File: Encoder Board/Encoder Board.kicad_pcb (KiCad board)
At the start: 2 copper layers, 62.2 x 52.8 mm, 20 parts, among them J1 Conn_02x05_Odd_Even, J2 Conn_02x05_Odd_Even, J3 Conn_01x02_Pin, J4 Conn_01x02_Pin, J5 Conn_01x20, J6 Conn_01x20, J7 Conn_02x04_Odd_Even, U1 AM26LV32xD

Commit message: routing
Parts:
- moved C1 2.41 mm to (68.5, 51.2)
- moved R1 1.97 mm to (65.4, 52.1)
- moved C4 0.72 mm to (75.1, 54.3)
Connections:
- C2 pad 1: /B_N -> /INDEX_N
- C3 pad 1: /INDEX_N -> /B_N
- J5 pad 5: /B_3V3 -> /INDEX_3V3
- J5 pad 6: /INDEX_3V3 -> /B_3V3
- R2 pad 2: /B -> /INDEX
- R3 pad 2: /INDEX -> /B
- U1 pad 10: /INDEX -> /B
- U1 pad 11: /INDEX_3V3 -> /B_3V3
- U1 pad 5: /B_3V3 -> /INDEX_3V3
- U1 pad 6: /B -> /INDEX
- U1 pad 7: /B_N -> /INDEX_N
- U1 pad 9: /INDEX_N -> /B_N
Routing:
- net /B_N: track 48.7 -> 97.4 mm, vias 0 -> 1
- net /B: track 54.3 -> 97.1 mm, vias 0 -> 1
- net /A: track 62.0 -> 83.5 mm
- net /INDEX_3V3: track 5.75 -> 24.5 mm, vias 0 -> 2
- net /INDEX_N: track 61.1 -> 77.9 mm
- net /INDEX: track 68.6 -> 80.5 mm
- net /A_3V3: track 14.9 -> 23.6 mm, vias 1 -> 2
- net /A_N: track 67.3 -> 73.2 mm
- net +3V3: track 1.14 -> 6.99 mm
- net /B_3V3: track 14.1 -> 18.5 mm
- net GND: track 2.54 -> 0.00 mm, vias 38 -> 37

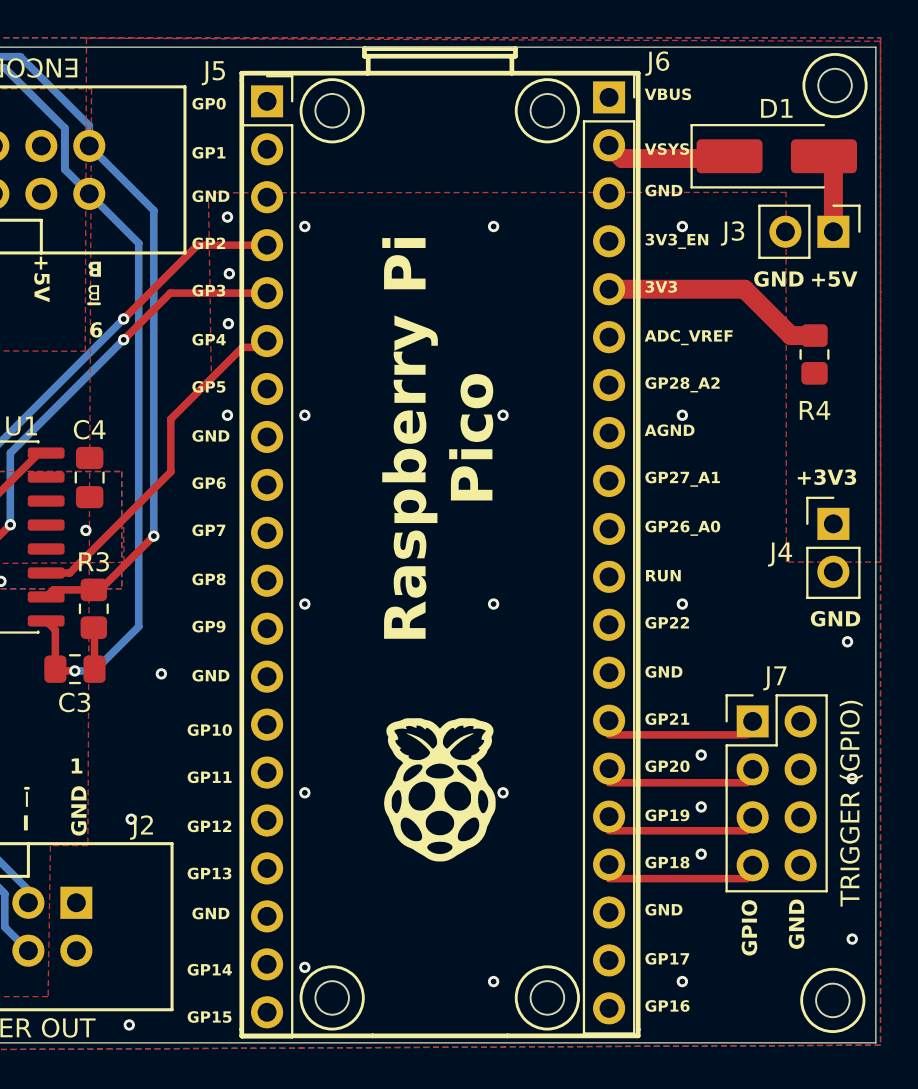
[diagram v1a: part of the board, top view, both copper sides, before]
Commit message: fix silkscreen
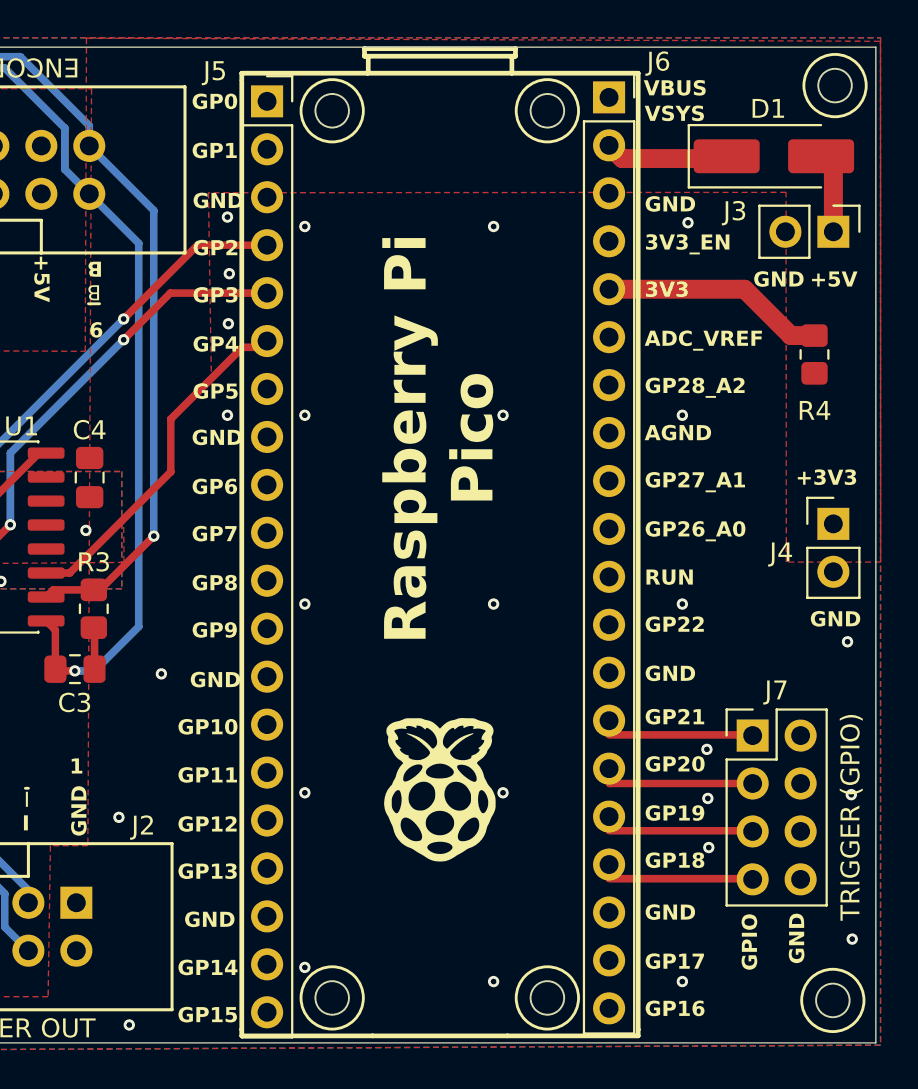
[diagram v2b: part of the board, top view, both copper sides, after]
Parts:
- moved J7 0.75 mm to (110.2, 68.0)
- moved D1 0.15 mm to (111.3, 37.3)
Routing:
- net Net-(J6-Pin_15): track 7.36 -> 7.94 mm

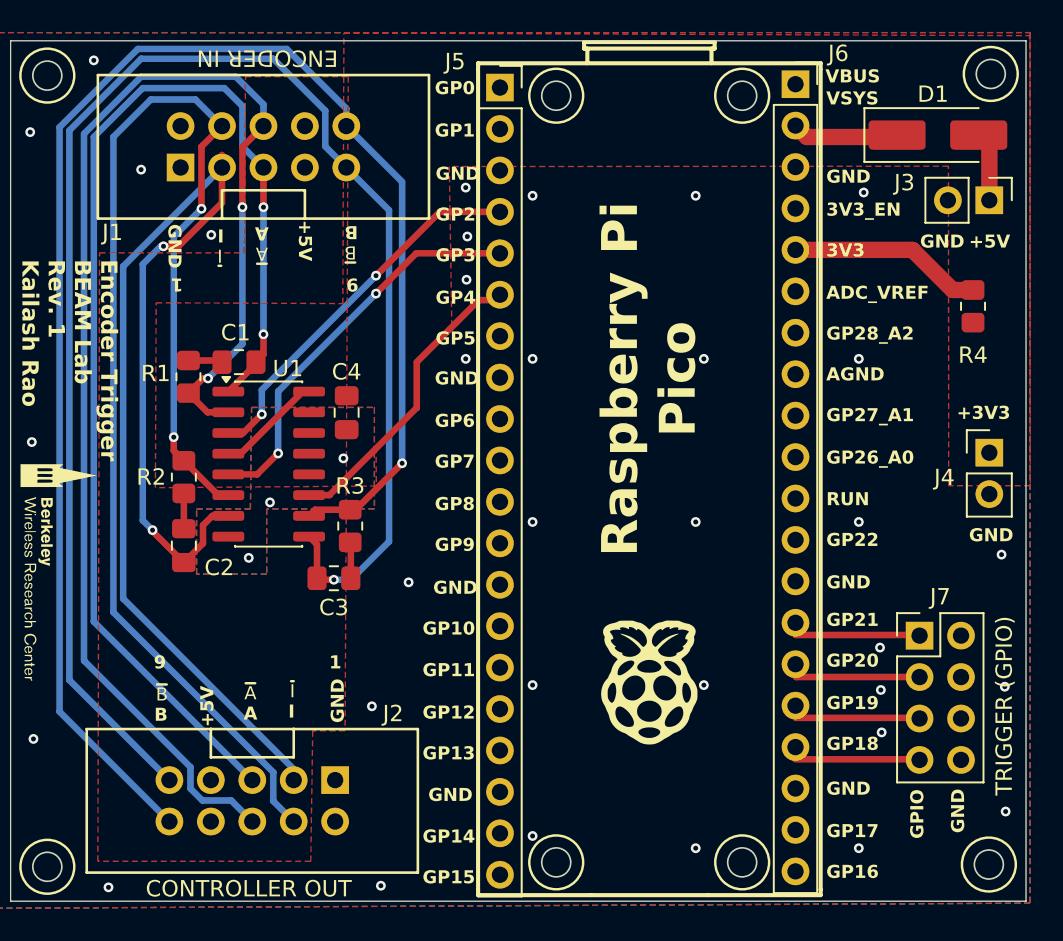
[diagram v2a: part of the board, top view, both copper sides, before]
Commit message: fix J7 connections, C4/U1 decoupling cap connection
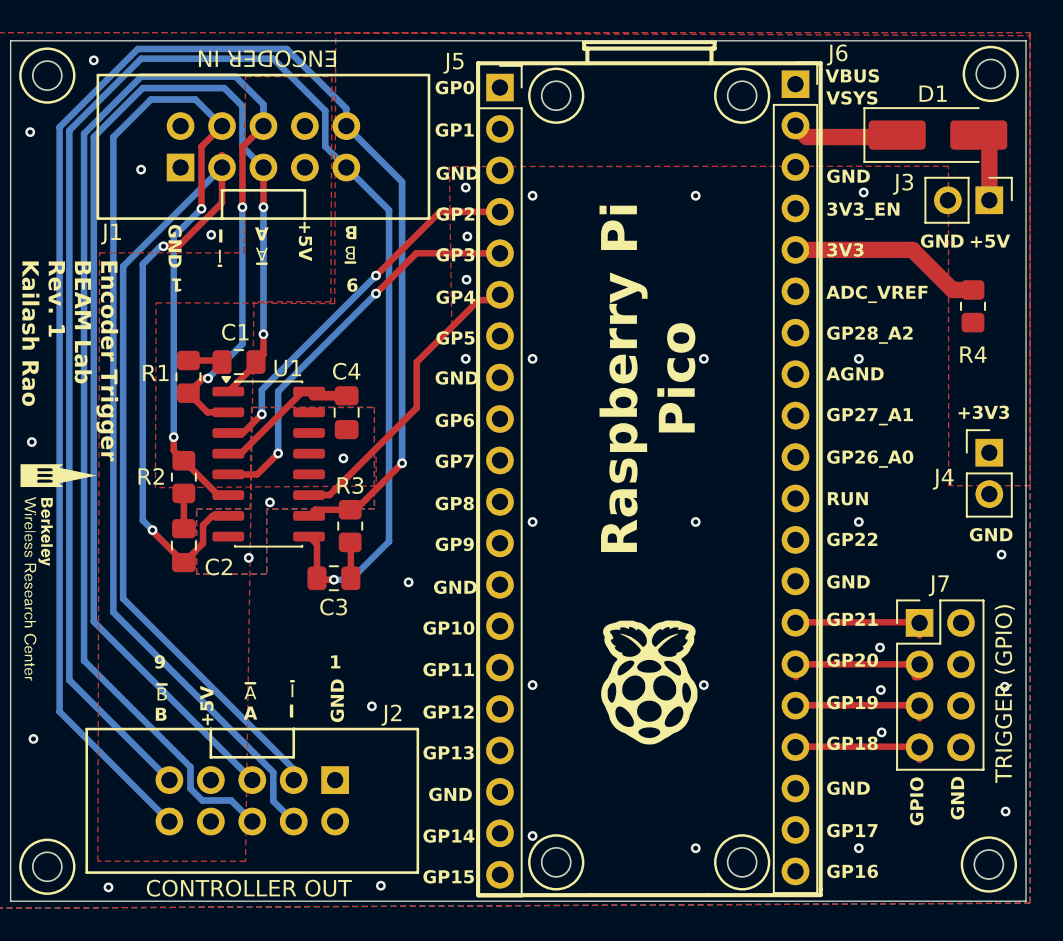
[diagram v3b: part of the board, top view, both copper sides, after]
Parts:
- moved J7 0.78 mm to (110.2, 67.2)
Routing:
- net +3V3: track 6.99 -> 9.40 mm
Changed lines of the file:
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@@
 	(footprint "Connector_PinHeader_2.54mm:PinHeader_2x04_P2.54mm_Vertical"
 		(layer "F.Cu")
-		(at 110.225 67.968)
+		(at 110.225 67.19)
 		(descr "Through hole straight pin header, 2x04, 2.54mm pitch, double rows")
 		(tags "Through hole pin header THT 2x04 2.54mm double row")
@@
 	)
 	(gr_text "GPIO"
-		(at 110.55 80.428 90)
+		(at 110.55 79.65 90)
 		(layer "F.SilkS")
 		(effects
@@
 	)
 	(gr_text "GND\n"
-		(at 113.05 80.078 90)
+		(at 113.05 79.3 90)
 		(layer "F.SilkS")
 		(effects
@@
 	)
 	(gr_text "TRIGGER (GPIO)"
-		(at 116 77.778 90)
+		(at 116 77 90)
 		(layer "F.SilkS")
 		(effects
@@
 	)
 	(segment
-		(start 102.617622 67.930806)
-		(end 110.187806 67.930806)
+		(start 102.617622 67.180806)
+		(end 102.645622 67.152806)
+		(width 0.4)
+		(layer "F.Cu")
+		(net "/TRIGGER")
+	)
+	(segment
+		(start 102.645622 67.152806)
+		(end 110.187806 67.152806)
 		(width 0.4)
 		(layer "F.Cu")
@@
 	)
 	(segment
-		(start 102.654816 70.508)
-		(end 110.225 70.508)
+		(start 102.654816 69.73)
+		(end 110.225 69.73)
 		(width 0.4)
 		(layer "F.Cu")
@@
 	)
 	(segment
-		(start 102.617622 73.010806)
-		(end 110.187806 73.010806)
+		(start 102.617622 72.232806)
+		(end 110.187806 72.232806)
 		(width 0.4)
 		(layer "F.Cu")
@@
 	)
 	(segment
-		(start 102.617622 75.550806)
-		(end 110.187806 75.550806)
+		(start 102.617622 74.772806)
+		(end 110.187806 74.772806)
 		(width 0.4)
 		(layer "F.Cu")
@@
 	)
 	(segment
+		(start 75.1 53.2625)
+		(end 73.0525 53.2625)
+		(width 0.6)
+		(layer "F.Cu")
+		(net "+3V3")
+	)
+	(segment
 		(start 72.795 53.005)
 		(end 72.335 53.005)
@@
 	)
 	(segment
+		(start 73.0525 53.2625)
+		(end 72.795 53.005)
+		(width 0.4)
+		(layer "F.Cu")
+		(net "+3V3")
+	)
+	(segment
 		(start 67.845 56.815)
 		(end 68.601264 56.815)
@@
 			(pts
 				(xy 81.393586 39.210744) (xy 81.55 49.15) (xy 79.4 51.2) (xy 79.4 54) (xy 76.900818 56.413811) (xy 76.919136 58.795762)
-				(xy 63.375514 58.899914) (xy 63.422562 47.563571) (xy 74.867387 47.611077) (xy 74.932481 31.022242)
+				(xy 63.375514 58.899914) (xy 63.422562 47.563571) (xy 74.367406 47.609013) (xy 74.4325 31.020268)
 				(xy 116.994215 31.187296) (xy 117.008019 58.777208) (xy 112.009037 58.778788) (xy 111.99368 39.189878)
 			)
@@
 		(polygon
 			(pts
-				(xy 75.199277 33.7) (xy 75.006024 73.8) (xy 73.021212 73.8) (xy 72.9 81.8) (xy 59.848334 81.8) (xy 59.951946 44.5)
-				(xy 68.810744 44.5) (xy 68.9 33.7)
+				(xy 74.199277 33.7) (xy 74.132771 47.5) (xy 69.419764 47.5) (xy 68.900068 81.8) (xy 59.848334 81.8)
+				(xy 59.951946 44.5) (xy 68.810744 44.5) (xy 68.9 33.7)
 			)
 		)

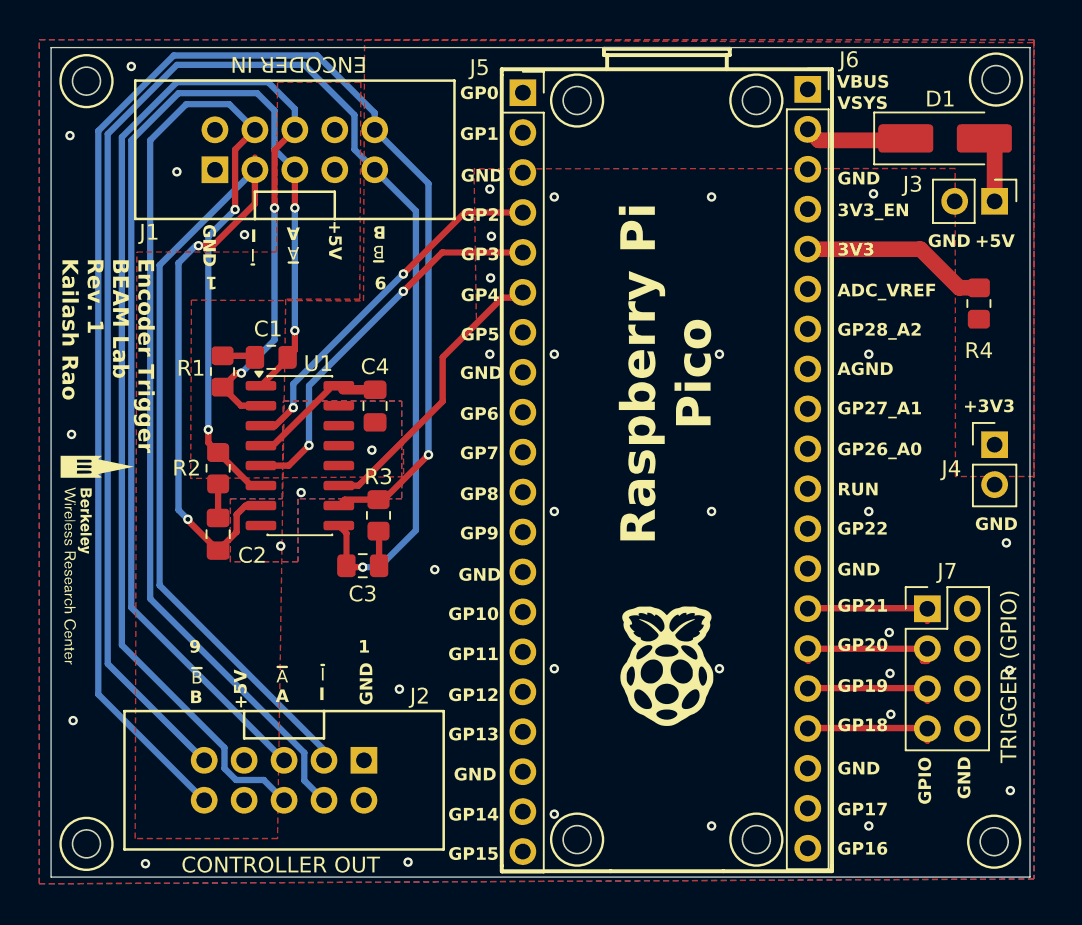
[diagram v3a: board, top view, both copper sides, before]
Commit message: Add more space for mounting holes
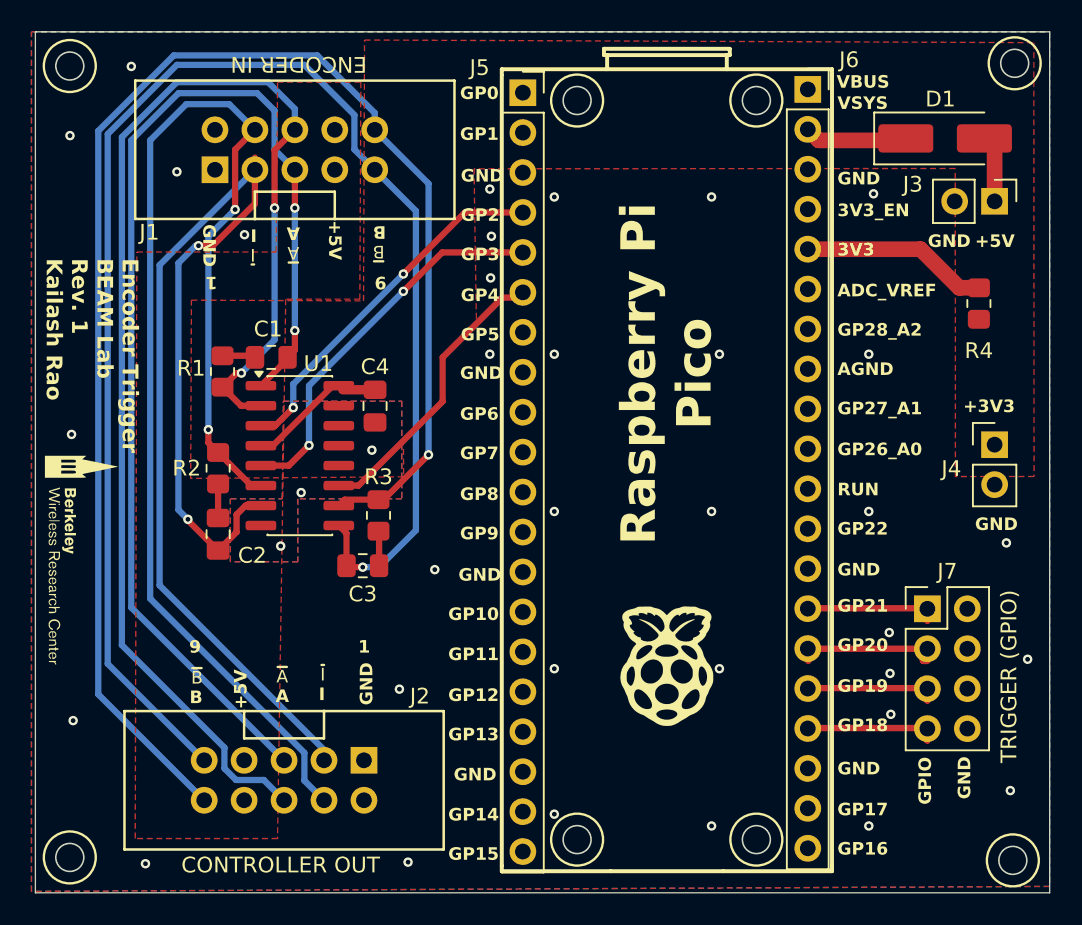
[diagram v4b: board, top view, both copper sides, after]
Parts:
- moved G*** 1.00 mm to (56.6, 64.0)
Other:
- board size 62.2 x 52.8 mm -> 64.5 x 54.8 mm
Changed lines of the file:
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@@
 	(footprint "LOGO"
 		(layer "F.Cu")
-		(at 57.6 64 -90)
+		(at 56.6 64 -90)
 		(property "Reference" "G***"
 			(at 0 0 90)
@@
 	)
 	(gr_circle
-		(center 56.75 33.634166)
-		(end 58.401 33.634166)
+		(center 55.689 32.673166)
+		(end 57.34 32.673166)
 		(stroke
 			(width 0.15)
@@
 	)
 	(gr_circle
-		(center 56.75 82.139)
-		(end 58.401 82.139)
+		(center 55.689 83)
+		(end 57.34 83)
 		(stroke
 			(width 0.15)
@@
 	)
 	(gr_circle
-		(center 114.472 82)
-		(end 116.123 82)
+		(center 115.65975 83.187834)
+		(end 117.31075 83.187834)
 		(stroke
 			(width 0.15)
@@
 	)
 	(gr_circle
-		(center 114.589 33.534166)
-		(end 116.24 33.534166)
+		(center 115.77675 32.5)
+		(end 117.42775 32.5)
 		(stroke
 			(width 0.15)
@@
 	)
 	(gr_rect
-		(start 54.5 31.5)
-		(end 116.75 84.25)
+		(start 53.5 30.5)
+		(end 118 85.25)
 		(radius 2)
 		(stroke
@@
 	)
 	(gr_circle
-		(center 56.75 33.634166)
-		(end 57.639 33.634166)
+		(center 55.689 32.673166)
+		(end 56.578 32.673166)
 		(stroke
 			(width 0.1)
@@
 	)
 	(gr_circle
-		(center 56.75 82.139)
-		(end 57.639 82.139)
+		(center 55.689 83)
+		(end 56.578 83)
 		(stroke
 			(width 0.1)
@@
 	)
 	(gr_circle
-		(center 114.472 82)
-		(end 115.361 82)
+		(center 115.65975 83.187834)
+		(end 116.54875 83.187834)
 		(stroke
 			(width 0.1)
@@
 	)
 	(gr_circle
-		(center 114.589 33.534166)
-		(end 115.478 33.534166)
+		(center 115.77675 32.5)
+		(end 116.66575 32.5)
 		(stroke
 			(width 0.1)
@@
 	)
 	(gr_text "Encoder Trigger\nBEAM Lab\nRev. 1\nKailash Rao"
-		(at 55.1 44.9 270)
+		(at 54.1 44.9 270)
 		(layer "F.SilkS")
 		(effects
@@
 	)
 	(via
-		(at 115.45 71.1)
+		(at 116.6 70.4)
 		(size 0.6)
 		(drill 0.3)
@@
 		(polygon
 			(pts
-				(xy 116.367 35.312166) (xy 112.811 35.312166) (xy 112.811 31.756166) (xy 116.367 31.756166)
+				(xy 117.55475 34.278) (xy 113.99875 34.278) (xy 113.99875 30.722) (xy 117.55475 30.722)
 			)
 		)
@@
 		(polygon
 			(pts
-				(xy 53.75 31.000326) (xy 117 30.999678) (xy 117 84.3696) (xy 53.75 84.68019)
+				(xy 53.25 30.500948) (xy 118 30.499672) (xy 118 84.842864) (xy 53.25 85.160209)
 			)
 		)
@@
 		(polygon
 			(pts
-				(xy 58.528 83.917) (xy 54.972 83.917) (xy 54.972 80.361) (xy 58.528 80.361)
+				(xy 57.467 84.778) (xy 53.911 84.778) (xy 53.911 81.222) (xy 57.467 81.222)
 			)
 		)
@@
 		(polygon
 			(pts
-				(xy 116.25 83.75) (xy 112.694 83.75) (xy 112.694 80.194) (xy 116.25 80.194)
+				(xy 117.43775 84.937834) (xy 113.88175 84.937834) (xy 113.88175 81.381834) (xy 117.43775 81.381834)
 			)
 		)
@@
 		(polygon
 			(pts
-				(xy 58.528 35.412166) (xy 54.972 35.412166) (xy 54.972 31.856166) (xy 58.528 31.856166)
+				(xy 57.467 34.451166) (xy 53.911 34.451166) (xy 53.911 30.895166) (xy 57.467 30.895166)
 			)
 		)
@@
 	)
 	(group ""
+		(members "93fe217f-e595-4d88-a985-b051b4b92898" "d4543a5d-1352-47ca-b8ab-cd00b801052e")
+	)
+	(group ""

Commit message: final gerbers
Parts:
- moved G*** 3.80 mm to (56.6, 67.8)
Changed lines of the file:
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@@
 	(footprint "LOGO"
 		(layer "F.Cu")
-		(at 56.6 64 -90)
+		(at 56.6 67.8 -90)
 		(property "Reference" "G***"
 			(at 0 0 90)
@@
 	)
 	(gr_text "Encoder Trigger\nBEAM Lab\nRev. 1\nKailash Rao"
-		(at 54.1 44.9 270)
+		(at 54.1 46.9 270)
 		(layer "F.SilkS")
 		(effects
@@
 		(polygon
 			(pts
-				(xy 53.25 30.500948) (xy 118 30.499672) (xy 118 84.842864) (xy 53.25 85.160209)
+				(xy 53.25 30.500948) (xy 118 30.499672) (xy 118 85.441204) (xy 53.25 85.75855)
 			)
 		)
